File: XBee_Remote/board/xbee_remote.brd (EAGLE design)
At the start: 96.5 x 64.8 mm, 39 parts, among them IC1 AVR-MEGA8-PPTH, IC2 74LS125N, IC5 74LS595N, J1 1X2-3.5MM, J2 AVR_SPI_PRG, Y1 RESONATORPTH

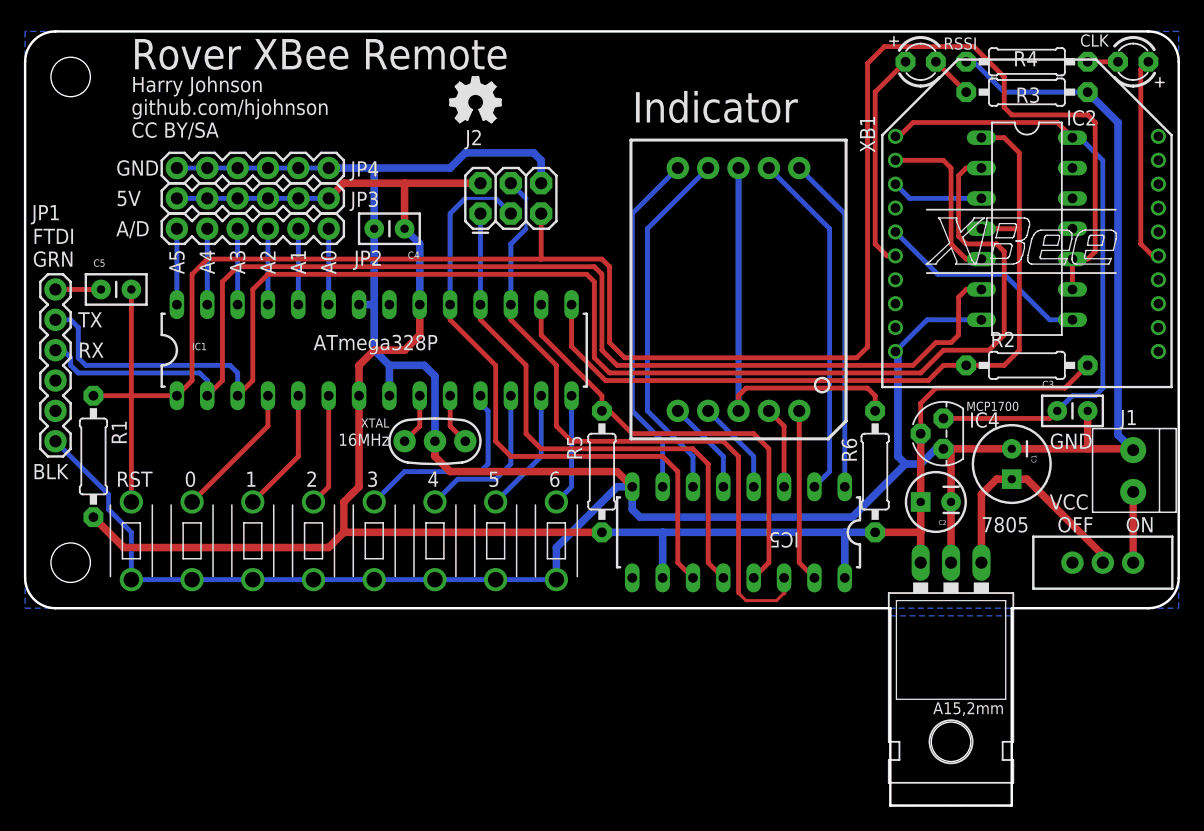
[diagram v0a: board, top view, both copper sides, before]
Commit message: New revision of remote: Added joystick, shifted parts.
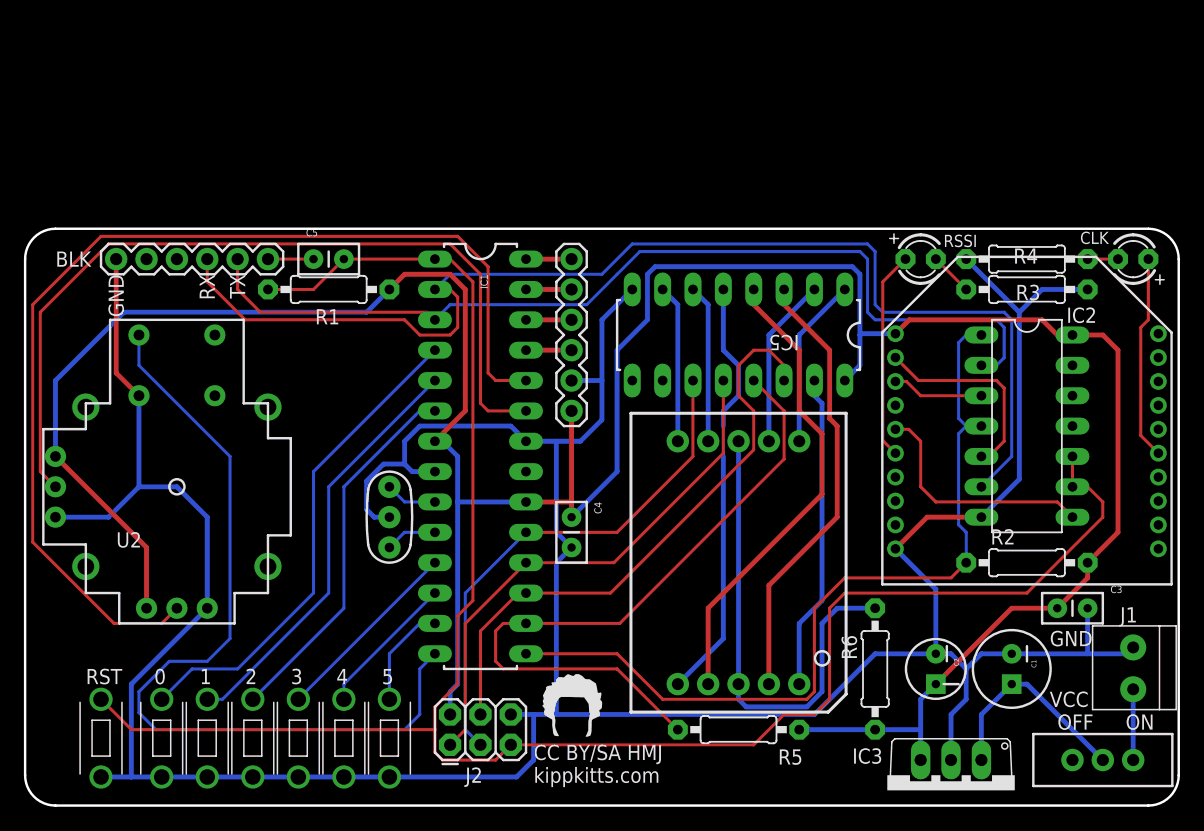
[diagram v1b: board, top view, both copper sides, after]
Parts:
- removed IC4: (no value), adafruit:TO92
- removed JP2, JP4: (no value), SparkFun:1X06
- removed JP5, JP6: STAND-OFF, SparkFun:STAND-OFF
- removed LOGO1: OSHW_LOGO_FILLX0150-NT, OSHW:OSHW_FILLX150_NOTEXT
- removed U$15: TACT_TL1107, customswitch:TACT_TL1107
- added U$2: (no value), KippkittsLogo:TOP_DOCU_5MM
- added U2: JOYSTICKPTH, SparkFun:JOYSTICK
- C1: value (none) -> 100uF
- C2: value (none) -> 10uF
- IC3: value (none) -> UA78M33CKCS; device SparkFun:78XXL -> linear:TO220V
- J2: value AVR_SPI_PRG -> AVR ICSP
- XB1: device maxstream:XBEE -> hjohnson_library:XBEE
- moved J2 44.5 mm to (35.6, 5.08)
- moved JP3 37.5 mm to (45.7, 33.0), turned to 90 degrees
- moved C4 27.9 mm to (45.7, 24.1), turned to 270 degrees
- moved R5 24.4 mm to (59.7, 6.35), turned to 0 degrees
- moved R1 24.1 mm to (25.4, 43.2), turned to 0 degrees
- moved U$4 22.9 mm to (59.7, 20.3)
- moved U$14 18.8 mm to (30.5, 8.89)
- moved U$13 18.2 mm to (26.7, 8.89)
- moved C5 18.0 mm to (24.1, 45.7)
- moved JP1 18.0 mm to (20.3, 45.7), turned to 180 degrees
- moved U$12 17.7 mm to (22.9, 8.89)
- moved U$11 17.3 mm to (19.1, 8.89)
- moved C1 17.1 mm to (82.5, 11.4)
- moved U$10 16.9 mm to (15.2, 8.89)
- moved U$8 16.7 mm to (6.35, 8.89)
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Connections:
- net /XBEE_ENABLE renamed /XBEE_EN
- net LATCHENABLE renamed 7_SEG_ENABLE
- removed net 5V: C2.1, C4.1, IC1.20, IC1.7, IC3.OUT, IC4.2, IC5.10, IC5.16, J2.2, JP3.1, JP3.2, JP3.3, JP3.4, JP3.5, JP3.6, R1.2, R2.2, R5.2, R6.1
- removed net A0: IC1.23, JP2.1
- removed net A1: IC1.24, JP2.2
- removed net IO6: IC1.14, U$15.1
- removed net N$5: C1.1, IC3.IN, S1.2
- new net IO_SEL: IC1.14, U2.B1A
- new net VIN: C1.1, IC3.1, S1.2
- new net VIN_H: IC1.24, U2.H2
- new net VIN_V: IC1.23, U2.V2
- net 3.3V: now also C2.1, C4.1, IC1.20, IC1.7, IC3.3, IC5.16, J2.2, JP3.1, R1.2, R2.2, R5.2, R6.1, U2.H1, U2.V1; no longer IC4.3
- net A2: now also JP3.3; no longer JP2.3
- net A3: now also JP3.4; no longer JP2.4
- net GND: now also IC3.2, JP3.2, U2.B2A, U2.H3, U2.V3; no longer IC3.GND, IC4.1, JP4.1, JP4.2, JP4.3, JP4.4, JP4.5, JP4.6, U$15.2
- net SCL: now also JP3.6; no longer JP2.6
- net SDA: now also JP3.5; no longer JP2.5
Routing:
- net 3.3V: track 52.6 -> 244.5 mm
- net 5V: track 166.8 -> 0.00 mm
- net VIN_H: track 0.00 -> 89.1 mm
- net VIN_V: track 0.00 -> 70.2 mm
- net IO_SEL: track 0.00 -> 70.0 mm
- net TX: track 120.3 -> 80.0 mm
- net 2: track 7.93 -> 39.3 mm
- net 4: track 6.88 -> 37.2 mm
- net IO0: track 11.5 -> 40.9 mm
- net 1: track 7.93 -> 35.7 mm
- net IO1: track 10.5 -> 35.3 mm
- net GND: track 263.5 -> 286.5 mm
- net IO2: track 9.42 -> 31.2 mm
- net 7_SEG_ENABLE: track 37.6 -> 57.9 mm
- net N$5: track 19.7 -> 0.00 mm
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- removed copper zone on layer 16, net GND
- removed copper zone on layer 16, net N$3
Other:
- board size 96.5 x 64.8 mm -> 96.5 x 48.3 mm
- board text added: "CC BY/SA HMJ"
- board text added: "kippkitts.com"
- board text removed: "16MHz"
- board text removed: "5V"
- board text removed: "6"
- board text removed: "7805"
- board text removed: "A/D"
- board text removed: "A0"
- board text removed: "A1"
- board text removed: "A2"
- board text removed: "A3"
- board text removed: "A4"
- board text removed: "A5"
- board text removed: "ATmega328P"
- board text removed: "CC BY/SA"
- board text removed: "FTDI"
- board text removed: "GRN"
- board text removed: "Harry Johnson"
- board text removed: "Indicator"
- board text removed: "MCP1700"
- board text removed: "Rover XBee Remote"
- board text removed: "XTAL"
- board text removed: "github.com/hjohnson"
